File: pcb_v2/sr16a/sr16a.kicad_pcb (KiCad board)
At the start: 2 copper layers, 61 x 9.2 mm, 39 parts, among them J1 Conn_02x22_Top_Bottom, U1 74LS193, U2 74LS193, U3 74LS193, U4 74LS193, U5 74LS244, U6 74LS244, U7 74LS244, U8 74LS244

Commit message: arquivos no note
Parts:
- removed D10, D11, D12, D9: 1N4148, Diode_THT:D_DO-35_SOD27_P7.62mm_Horizontal
- removed R10, R9: 10K, Resistor_THT:R_Axial_DIN0207_L6.3mm_D2.5mm_P7.62mm_Horizontal
- added C9: 100nF, Capacitor_THT:C_Disc_D5.1mm_W3.2mm_P5.00mm, F.Cu at (155.6, 64.7)
- added U9: 74LS32, Package_DIP:DIP-14_W7.62mm, F.Cu at (159.4, 67.3)
- moved U1 103.1 mm to (156.8, 100.3), turned to 90 degrees
- moved C1 96.9 mm to (153.0, 97.7), turned to 90 degrees
- moved C5 62.7 mm to (113.7, 78.8), turned to -90 degrees
- moved U5 58.9 mm to (109.9, 76.2), turned to -90 degrees
- moved C8 57.9 mm to (76.8, 95.3), turned to -90 degrees
- moved U8 53.9 mm to (73.0, 92.7), turned to -90 degrees
- moved U2 51.5 mm to (125.1, 83.8), turned to 90 degrees
- moved C7 49.0 mm to (113.7, 95.3), turned to -90 degrees
- moved U4 46.5 mm to (156.8, 83.8), turned to 90 degrees
- moved C2 45.1 mm to (121.3, 81.2), turned to 90 degrees
- moved U7 42.6 mm to (109.9, 92.7), turned to -90 degrees
- moved R4 42.2 mm to (87.0, 68.6), turned to 90 degrees
- moved C4 40.0 mm to (153.1, 81.2), turned to 90 degrees
- moved U3 35.6 mm to (125.1, 100.3), turned to 90 degrees
- moved D8 33.7 mm to (122.6, 64.1)
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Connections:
- J1 pad 5: unconnected-(J1-Pad5) -> ~{clock}
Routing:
- net ~{load_low}: track 0.00 -> 109.0 mm, vias 0 -> 3
- net addr_{4}: track 0.00 -> 68.0 mm, vias 0 -> 1
- net addr_{5}: track 0.00 -> 65.5 mm, vias 0 -> 1
- net ~{addr_sel}: track 0.00 -> 64.9 mm, vias 0 -> 1
- net addr_{6}: track 0.00 -> 63.5 mm, vias 0 -> 1
- net addr_{3}: track 0.00 -> 63.2 mm, vias 0 -> 1
- net ~{load_high}: track 0.00 -> 62.5 mm, vias 0 -> 2
- net addr_{7}: track 0.00 -> 61.7 mm, vias 0 -> 1
- net data_{4}: track 0.00 -> 54.8 mm
- net addr_{2}: track 0.00 -> 53.5 mm, vias 0 -> 1
- net data_{5}: track 0.00 -> 51.9 mm
- net data_{6}: track 0.00 -> 50.6 mm
- net data_{0}: track 0.00 -> 48.2 mm
- net data_{7}: track 0.00 -> 45.4 mm
- net addr_{1}: track 0.00 -> 44.9 mm, vias 0 -> 1
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- added copper zone on B.Cu, net GND
- added copper zone on F.Cu, net GND
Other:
- board size 61 x 9.2 mm -> 142.2 x 55.2 mm

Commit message: arquivos do gdrive
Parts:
- removed C9: 100nF, Capacitor_THT:C_Disc_D5.1mm_W3.2mm_P5.00mm
- removed U9: 74LS32, Package_DIP:DIP-14_W7.62mm
- added D10: 1N4148, Diode_THT:D_DO-35_SOD27_P7.62mm_Horizontal, F.Cu at (133.3, 61.0)
- added D11: 1N4148, Diode_THT:D_DO-35_SOD27_P7.62mm_Horizontal, F.Cu at (142.9, 61.0)
- added D12: 1N4148, Diode_THT:D_DO-35_SOD27_P7.62mm_Horizontal, F.Cu at (136.5, 61.0)
- added D9: 1N4148, Diode_THT:D_DO-35_SOD27_P7.62mm_Horizontal, F.Cu at (139.7, 61.0)
- added R10: 10K, Resistor_THT:R_Axial_DIN0207_L6.3mm_D2.5mm_P7.62mm_Horizontal, F.Cu at (149.2, 61.0)
- added R9: 10K, Resistor_THT:R_Axial_DIN0207_L6.3mm_D2.5mm_P7.62mm_Horizontal, F.Cu at (146.1, 61.0)
- moved C1 104.2 mm to (50.2, 81.2)
- moved U1 104.2 mm to (54.0, 83.8)
- moved U8 84.2 mm to (156.8, 100.3), turned to 90 degrees
- moved C8 76.2 mm to (153.0, 97.8), turned to 90 degrees
- moved C5 66.3 mm to (50.2, 97.7), turned to 90 degrees
- moved U5 60.9 mm to (54.0, 100.3), turned to 90 degrees
- moved C3 40.4 mm to (84.5, 81.3)
- moved U3 40.4 mm to (88.3, 83.8)
- moved U6 28.5 mm to (88.3, 100.3), turned to 90 degrees
- moved C6 20.4 mm to (84.5, 97.7), turned to 90 degrees
- moved U7 14.8 mm to (122.6, 100.3), turned to 90 degrees
- moved C7 5.64 mm to (118.7, 97.8), turned to 90 degrees
- moved C2 2.54 mm to (118.7, 81.2)
- moved U2 2.54 mm to (122.6, 83.8)
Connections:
- J1 pad 5: ~{clock} -> unconnected-(J1-Pad5)
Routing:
- net count_down: track 0.00 -> 110.5 mm, vias 0 -> 2
- net count_up: track 0.00 -> 104.6 mm, vias 0 -> 2
- net addr_{0}: track 37.6 -> 85.2 mm, vias 2 -> 0
- net ~{load_low}: track 109.0 -> 64.4 mm, vias 3 -> 1
- net addr_{1}: track 44.9 -> 88.2 mm, vias 1 -> 0
- net addr_{10}: track 15.7 -> 57.7 mm
- net ~{read_high}: track 0.00 -> 39.0 mm, vias 0 -> 2
- net addr_{2}: track 53.5 -> 91.0 mm, vias 1 -> 0
- net ~{read_low}: track 0.00 -> 36.5 mm, vias 0 -> 1
- net data_{7}: track 45.4 -> 81.0 mm, vias 0 -> 3
- net addr_{11}: track 26.9 -> 59.8 mm
- net addr_{3}: track 63.2 -> 93.7 mm, vias 1 -> 0
- net data_{6}: track 50.6 -> 80.3 mm, vias 0 -> 4
- net data_{0}: track 48.2 -> 23.3 mm
- net addr_{12}: track 31.6 -> 56.4 mm
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
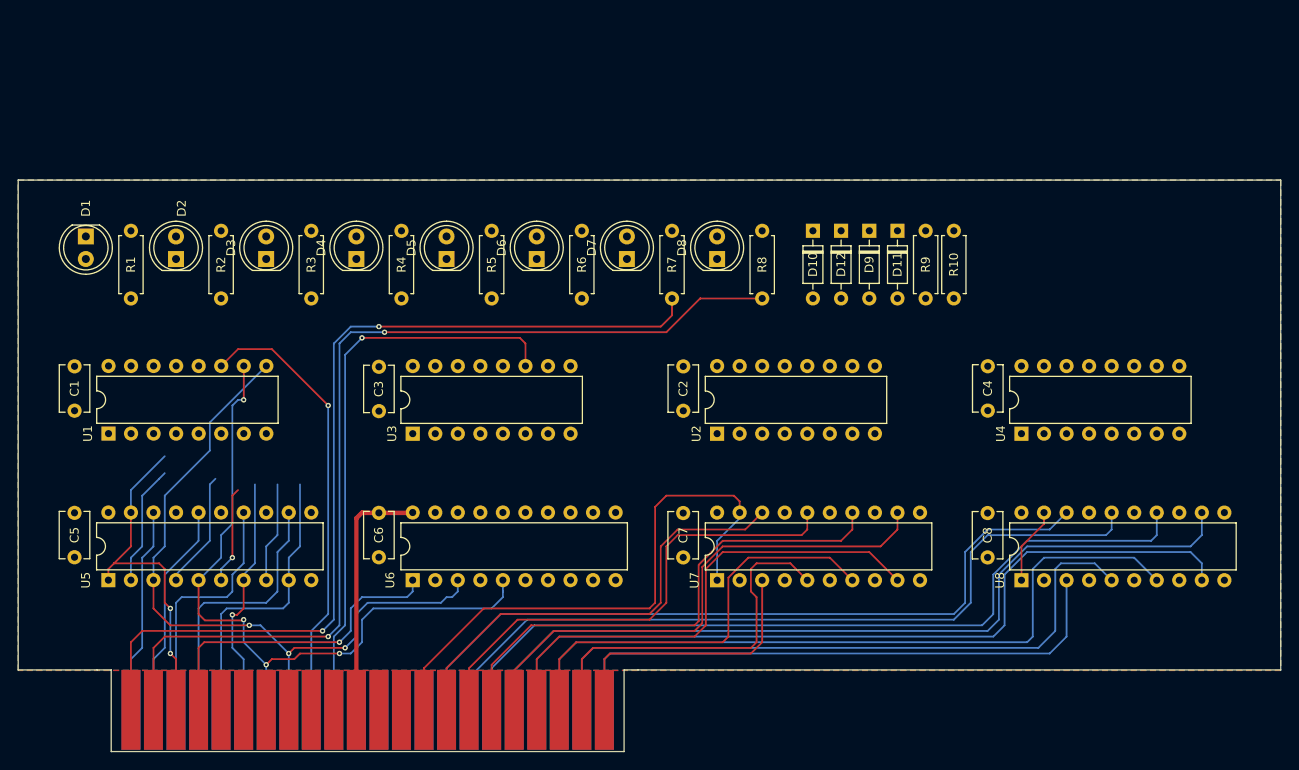
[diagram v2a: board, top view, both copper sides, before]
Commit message: adicionados o designador e o swap para a arquivo reg16
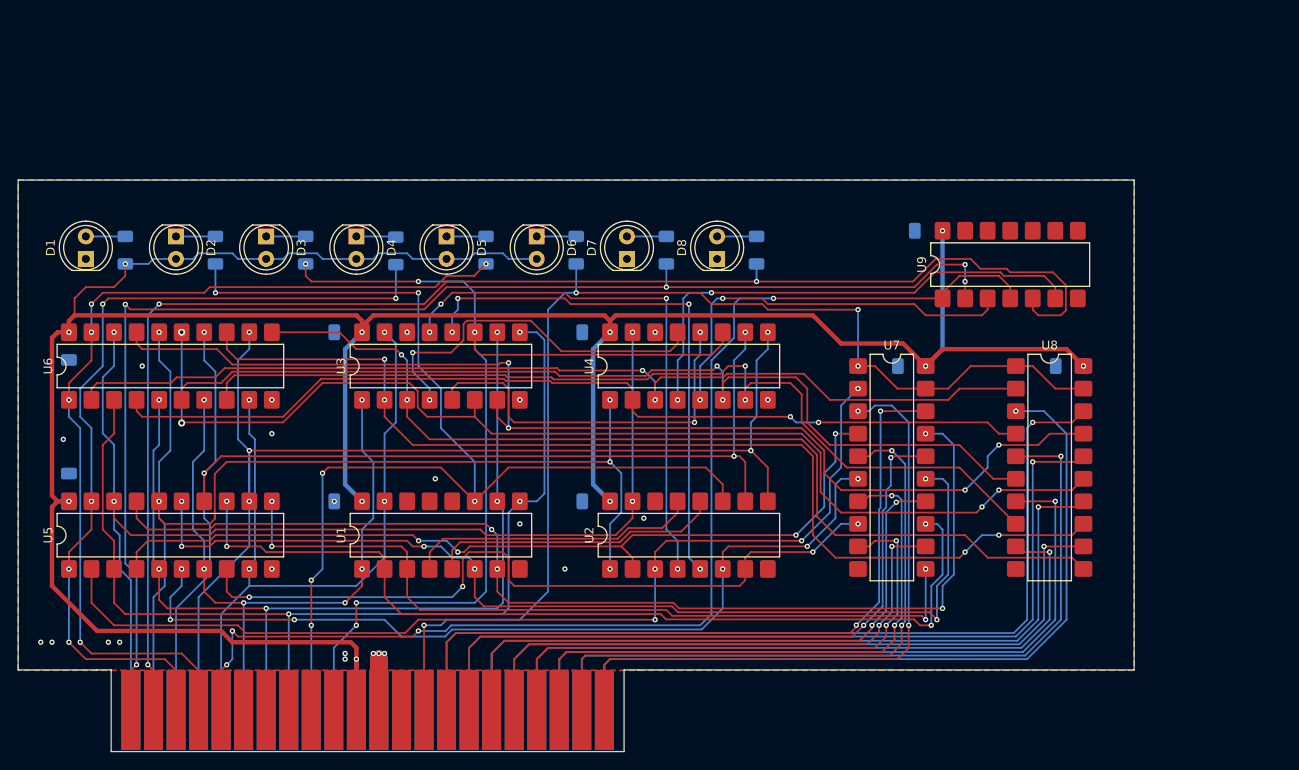
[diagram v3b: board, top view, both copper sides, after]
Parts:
- removed D10, D11, D12, D9: 1N4148, Diode_THT:D_DO-35_SOD27_P7.62mm_Horizontal
- removed R10, R9: 10K, Resistor_THT:R_Axial_DIN0207_L6.3mm_D2.5mm_P7.62mm_Horizontal
- added C9: 100nF, Capacitor_SMD:C_1206_3216Metric_Pad1.33x1.80mm_HandSolder, B.Cu at (146.4, 61.0)
- added U9: 74LS32, Package_DIP:SMDIP-14_W7.62mm, F.Cu at (155.6, 64.8)
- C1, C2, C3, C4, C5, C6, C7, C8: footprint Capacitor_THT:C_Disc_D5.1mm_W3.2mm_P5.00mm -> Capacitor_SMD:C_1206_3216Metric_Pad1.33x1.80mm_HandSolder; moved to B.Cu
- R1, R2, R3, R4, R5, R6, R7, R8: footprint Resistor_THT:R_Axial_DIN0207_L6.3mm_D2.5mm_P7.62mm_Horizontal -> Resistor_SMD:R_1206_3216Metric_Pad1.30x1.75mm_HandSolder; moved to B.Cu
- U1, U2, U3, U4: footprint Package_DIP:DIP-16_W7.62mm -> Package_DIP:SMDIP-16_W7.62mm
- U5, U6, U7, U8: footprint Package_DIP:DIP-20_W7.62mm -> Package_DIP:SMDIP-20_W7.62mm
- moved C4 45.0 mm to (108.9, 72.4), turned to 0 degrees
- moved C6 42.3 mm to (49.5, 74.0)
- moved U1 39.2 mm to (91.4, 95.2)
- moved U4 38.2 mm to (119.4, 76.2)
- moved U6 36.4 mm to (61.0, 76.2)
- moved C7 33.6 mm to (144.5, 76.2), turned to 0 degrees
- moved C1 32.5 mm to (81.0, 91.4), turned to 0 degrees
- moved C8 23.5 mm to (162.3, 76.2), turned to 0 degrees
- moved U7 23.4 mm to (142.2, 87.6), turned to 0 degrees
- moved C2 14.2 mm to (108.9, 91.4), turned to 0 degrees
- moved U8 13.1 mm to (160.0, 87.6), turned to 0 degrees
- moved U2 11.9 mm to (119.4, 95.2)
- moved C3 9.54 mm to (81.0, 72.4), turned to 0 degrees
- moved U5 8.63 mm to (61.0, 95.2)
- moved U3 8.25 mm to (91.4, 76.2)
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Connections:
- J1 pad 5: unconnected-(J1-Pad5) -> ~{clock}
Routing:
- net +5V: track 28.2 -> 322.0 mm, vias 0 -> 11
- net ~{clock}: track 0.00 -> 135.3 mm, vias 0 -> 4
- net count_{7}: track 0.00 -> 127.8 mm, vias 0 -> 4
- net count_{6}: track 0.00 -> 126.9 mm, vias 0 -> 4
- net count_{15}: track 0.00 -> 123.8 mm, vias 0 -> 4
- net count_{5}: track 0.00 -> 118.7 mm, vias 0 -> 4
- net count_{14}: track 0.00 -> 114.9 mm, vias 0 -> 6
- net count_{0}: track 0.00 -> 113.1 mm, vias 0 -> 2
- net count_{4}: track 0.00 -> 110.3 mm, vias 0 -> 2
- net count_{2}: track 0.00 -> 109.3 mm, vias 0 -> 2
- net count_{1}: track 0.00 -> 106.4 mm, vias 0 -> 2
- net count_{3}: track 0.00 -> 105.8 mm, vias 0 -> 2
- net data_{0}: track 23.3 -> 127.8 mm, vias 0 -> 4
- net count_{13}: track 0.00 -> 104.2 mm, vias 0 -> 4
- net data_{2}: track 28.4 -> 129.6 mm, vias 0 -> 4
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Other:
- board size 142.2 x 55.2 mm -> 125.7 x 55.2 mm

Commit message: concluido o desenho das placas satelite do banco de registradores de 16 bits
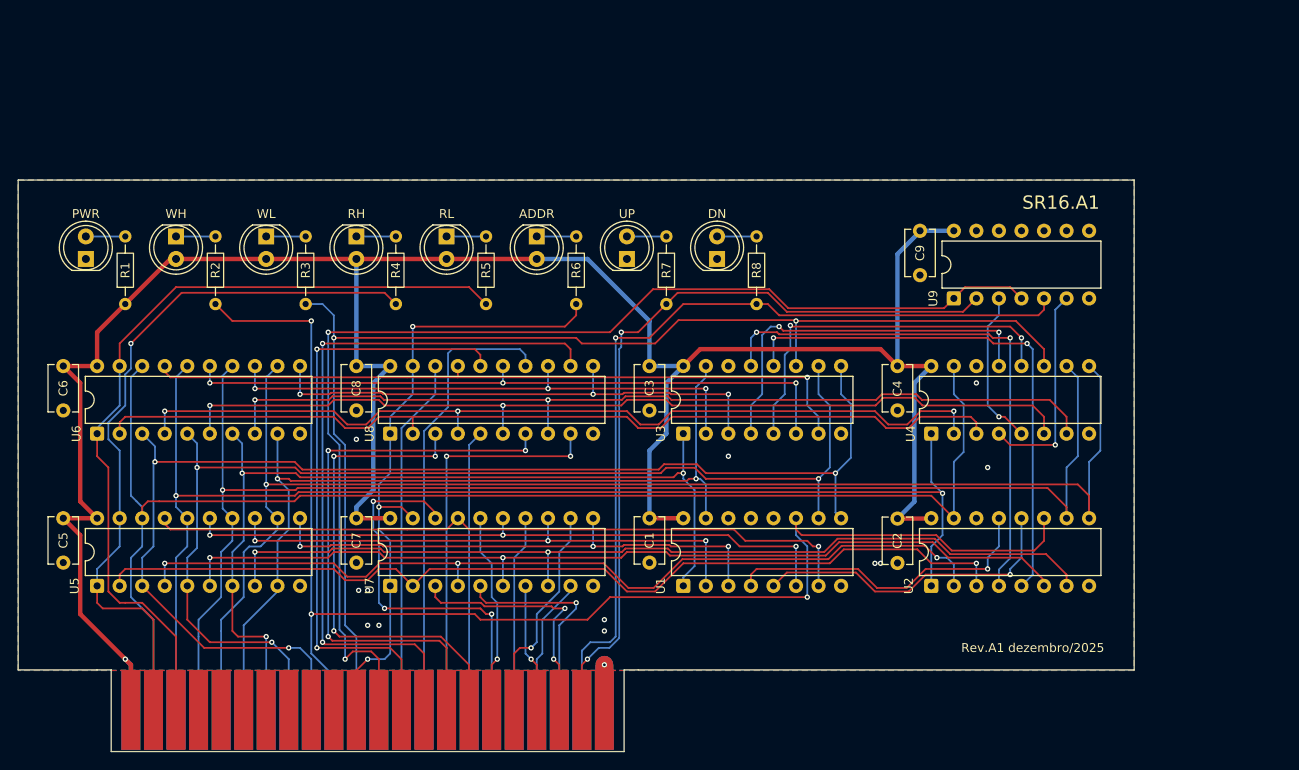
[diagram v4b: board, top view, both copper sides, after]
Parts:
- C1, C2, C3, C4, C5, C6, C7, C8, C9: footprint Capacitor_SMD:C_1206_3216Metric_Pad1.33x1.80mm_HandSolder -> Capacitor_THT:C_Disc_D5.1mm_W3.2mm_P5.00mm; moved to F.Cu
- D1: value LED -> PWR
- D2: value LED -> WH
- D3: value LED -> WL
- D4: value LED -> RH
- D5: value LED -> RL
- D6: value LED -> ADDR
- D7: value LED -> UP
- D8: value LED -> DN
- R1, R2, R3, R4, R5, R6, R7, R8: footprint Resistor_SMD:R_1206_3216Metric_Pad1.30x1.75mm_HandSolder -> Resistor_THT:R_Axial_DIN0204_L3.6mm_D1.6mm_P7.62mm_Horizontal; moved to F.Cu
- U1, U2, U3, U4: footprint Package_DIP:SMDIP-16_W7.62mm -> Package_DIP:DIP-16_W7.62mm
- U5, U6, U7, U8: footprint Package_DIP:SMDIP-20_W7.62mm -> Package_DIP:DIP-20_W7.62mm
- U9: footprint Package_DIP:SMDIP-14_W7.62mm -> Package_DIP:DIP-14_W7.62mm
- moved C8 80.5 mm to (81.9, 81.2), turned to 90 degrees
- moved U8 74.4 mm to (85.7, 83.8), turned to 90 degrees
- moved C7 66.4 mm to (81.9, 98.3), turned to 90 degrees
- moved U7 58.1 mm to (85.7, 101.0), turned to 90 degrees
- moved C3 35.1 mm to (114.9, 81.2), turned to 90 degrees
- moved C4 35.1 mm to (142.9, 81.2), turned to 90 degrees
- moved C2 34.7 mm to (142.9, 98.4), turned to 90 degrees
- moved C1 34.6 mm to (114.9, 98.3), turned to 90 degrees
- moved U4 28.3 mm to (146.7, 83.8)
- moved U3 28.3 mm to (118.7, 83.8)
- moved U1 27.9 mm to (118.7, 101.0)
- moved U2 27.9 mm to (146.7, 101.0)
- moved U6 11.2 mm to (52.7, 83.8)
- moved U5 10.0 mm to (52.7, 101.0)
- moved C5 8.49 mm to (48.9, 98.3), turned to 90 degrees
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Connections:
- J1 pad 1: count_up -> +5V
- J1 pad 11: +5V -> ~{addr_sel}
- J1 pad 12: GND -> ~{clock}
- J1 pad 13: unconnected-(J1-Pin_13-Pad13) -> addr_{1}
- J1 pad 14: ~{addr_sel} -> addr_{3}
- J1 pad 15: addr_{8} -> addr_{5}
- J1 pad 16: addr_{9} -> addr_{7}
- J1 pad 17: addr_{10} -> addr_{9}
- J1 pad 19: addr_{12} -> addr_{13}
- J1 pad 2: count_down -> ~{read_high}
- J1 pad 20: addr_{13} -> addr_{15}
- J1 pad 21: addr_{14} -> count_up
- J1 pad 22: addr_{15} -> GND
- J1 pad 23: data_{0} -> +5V
- J1 pad 24: data_{1} -> data_{0}
- J1 pad 25: data_{2} -> data_{1}
- J1 pad 26: data_{3} -> data_{2}
- J1 pad 27: data_{4} -> data_{3}
- J1 pad 28: data_{5} -> data_{4}
- J1 pad 29: data_{6} -> data_{5}
- J1 pad 3: ~{read_high} -> ~{read_low}
- J1 pad 30: data_{7} -> data_{6}
- J1 pad 31: ~{load_high} -> data_{7}
- J1 pad 32: ~{load_low} -> ~{load_high}
- J1 pad 33: +5V -> ~{load_low}
- J1 pad 34: GND -> unconnected-(J1-Pin_34-Pad34)
- J1 pad 35: unconnected-(J1-Pin_35-Pad35) -> addr_{0}
- J1 pad 36: unconnected-(J1-Pin_36-Pad36) -> addr_{2}
- J1 pad 37: addr_{0} -> addr_{4}
- J1 pad 38: addr_{1} -> addr_{6}
- J1 pad 39: addr_{2} -> addr_{8}
- J1 pad 4: ~{read_low} -> unconnected-(J1-Pin_4-Pad4)
- J1 pad 40: addr_{3} -> addr_{10}
- J1 pad 41: addr_{4} -> addr_{12}
- J1 pad 42: addr_{5} -> addr_{14}
- J1 pad 43: addr_{6} -> count_down
- J1 pad 44: addr_{7} -> GND
- J1 pad 5: ~{clock} -> unconnected-(J1-Pin_5-Pad5)
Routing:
- net count_down: track 162.2 -> 96.7 mm, vias 3 -> 1
- net addr_{0}: track 102.8 -> 40.3 mm, vias 1 -> 0
- net count_up: track 149.8 -> 88.4 mm, vias 5 -> 2
- net ~{addr_sel}: track 131.4 -> 72.5 mm, vias 4 -> 3
- net count_{5}: track 118.7 -> 61.0 mm, vias 4 -> 3
- net addr_{9}: track 76.6 -> 22.6 mm, vias 2 -> 1
- net addr_{6}: track 85.0 -> 31.6 mm, vias 1 -> 0
- net addr_{13}: track 65.8 -> 14.5 mm, vias 2 -> 1
- net count_{6}: track 126.9 -> 75.6 mm, vias 4 -> 3
- net count_{4}: track 110.3 -> 59.3 mm, vias 2 -> 3
- net +5V: track 322.0 -> 271.5 mm, vias 11 -> 1
- net addr_{10}: track 69.1 -> 22.1 mm, vias 2 -> 0
- net addr_{12}: track 62.1 -> 15.5 mm, vias 2 -> 0
- net count_{7}: track 127.8 -> 81.4 mm, vias 4 -> 1
- net addr_{14}: track 69.1 -> 25.2 mm, vias 2 -> 1
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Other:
- board text added: "Rev.A1 dezembro/2025"
- board text added: "SR16.A1"

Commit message: apenas questões estéticas
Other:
- board text added: "SR16"
- board text removed: "SR16.A1"
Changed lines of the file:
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@@
+	)
+	(gr_line
+		(start 43.815 110.435)
+		(end 43.815 55.245)
+		(stroke
+			(width 0.1)
+			(type default)
+		)
+		(layer "Edge.Cuts")
 	)
 	(gr_line
@@
 		(start 113.665 110.435)
 		(end 169.545 110.435)
-		(stroke
-			(width 0.1)
-			(type default)
-		)
-		(layer "Edge.Cuts")
-	)
-	(gr_line
-		(start 43.815 110.435)
-		(end 43.815 55.245)
 		(stroke
 			(width 0.1)
@@
 		)
 	)
-	(gr_text "SR16.A1"
-		(at 161.29 57.785 0)
+	(gr_text "SR16"
+		(at 163.83 57.785 0)
 		(layer "F.SilkS")
 		(effects
@@
 	)
 	(segment
-		(start 144.78 91.48)
-		(end 142.875 93.385)
+		(start 144.78 83.82)
+		(end 142.875 85.725)
 		(width 0.5)
 		(layer "B.Cu")
@@
 	)
 	(segment
-		(start 81.915 92.075)
-		(end 81.915 93.345)
-		(width 0.5)
-		(layer "B.Cu")
-		(net 2)
-	)
-	(segment
 		(start 107.95 64.135)
 		(end 102.235 64.135)
@@
 	)
 	(segment
+		(start 146.685 76.2)
+		(end 144.78 78.105)
+		(width 0.5)
+		(layer "B.Cu")
+		(net 2)
+	)
+	(segment
 		(start 118.745 76.195)
 		(end 116.84 78.1)
@@
 	)
 	(segment
-		(start 83.82 78.105)
-		(end 83.82 90.17)
-		(width 0.5)
-		(layer "B.Cu")
-		(net 2)
-	)
-	(segment
 		(start 114.935 76.2)
 		(end 114.935 71.12)
@@
 	)
 	(segment
+		(start 83.82 85.09)
+		(end 81.915 86.995)
+		(width 0.5)
+		(layer "B.Cu")
+		(net 2)
+	)
+	(segment
 		(start 85.725 76.2)
 		(end 83.82 78.105)
@@
 	)
 	(segment
-		(start 146.685 76.2)
-		(end 144.78 78.105)
-		(width 0.5)
-		(layer "B.Cu")
-		(net 2)
-	)
-	(segment
 		(start 114.935 93.385)
 		(end 114.935 93.345)
@@
 	(segment
 		(start 144.78 78.105)
-		(end 144.78 91.48)
+		(end 144.78 83.82)
 		(width 0.5)
 		(layer "B.Cu")
@@
 	)
 	(segment
-		(start 83.82 90.17)
-		(end 81.915 92.075)
-		(width 0.5)
-		(layer "B.Cu")
-		(net 2)
-	)
-	(segment
 		(start 56.515 109.855)
 		(end 55.88 109.22)
@@
 	)
 	(segment
+		(start 142.875 85.725)
+		(end 142.875 93.385)
+		(width 0.5)
+		(layer "B.Cu")
+		(net 2)
+	)
+	(segment
+		(start 83.82 78.105)
+		(end 83.82 85.09)
+		(width 0.5)
+		(layer "B.Cu")
+		(net 2)
+	)
+	(segment
 		(start 142.875 63.58)
 		(end 145.415 61.04)
 		(width 0.5)
 		(layer "B.Cu")
+		(net 2)
+	)
+	(segment
+		(start 81.915 86.995)
+		(end 81.915 93.345)
+		(width 0.5)
+		(layer "B.Cu")
